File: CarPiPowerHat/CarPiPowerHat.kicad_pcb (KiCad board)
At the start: 4 copper layers, 96 x 85 mm, 124 parts, among them IC1 AP2331TDSA-7, J1 HDMI_A_1.4, J10 Conn_01x02_Male, J2 1-84953-5, J3 40HAT, J4 Conn_02x03_Counter_Clockwise, J5 USB_A, J6 1-84953-5, J7 HDMI_A_1.4, J8 AudioJack2_Ground, J9 Conn_01x04, Q1 DMMT5401, Q2 DMG2305UX, Q3 DMP3013SFV-7, Q4 DMG2305, U1 AP64501SP-13, U2 CAT24C32, U3 LM3480-5.0, U4 ATtiny45V-10X, U5 PCF85063AT/AAZ, U7 AP2112-3.3K, U8 UDA1334ATS, Y1 X32K768S301

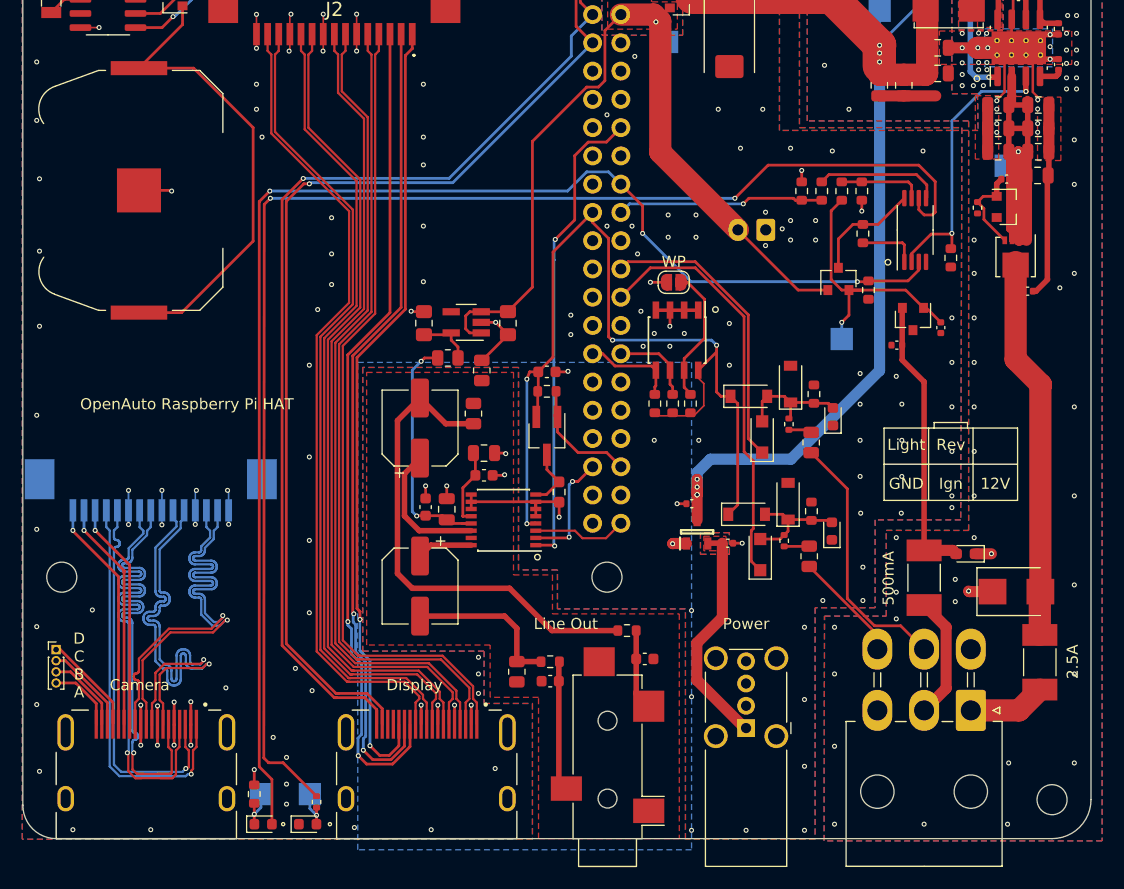
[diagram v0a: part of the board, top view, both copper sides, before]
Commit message: updated layout
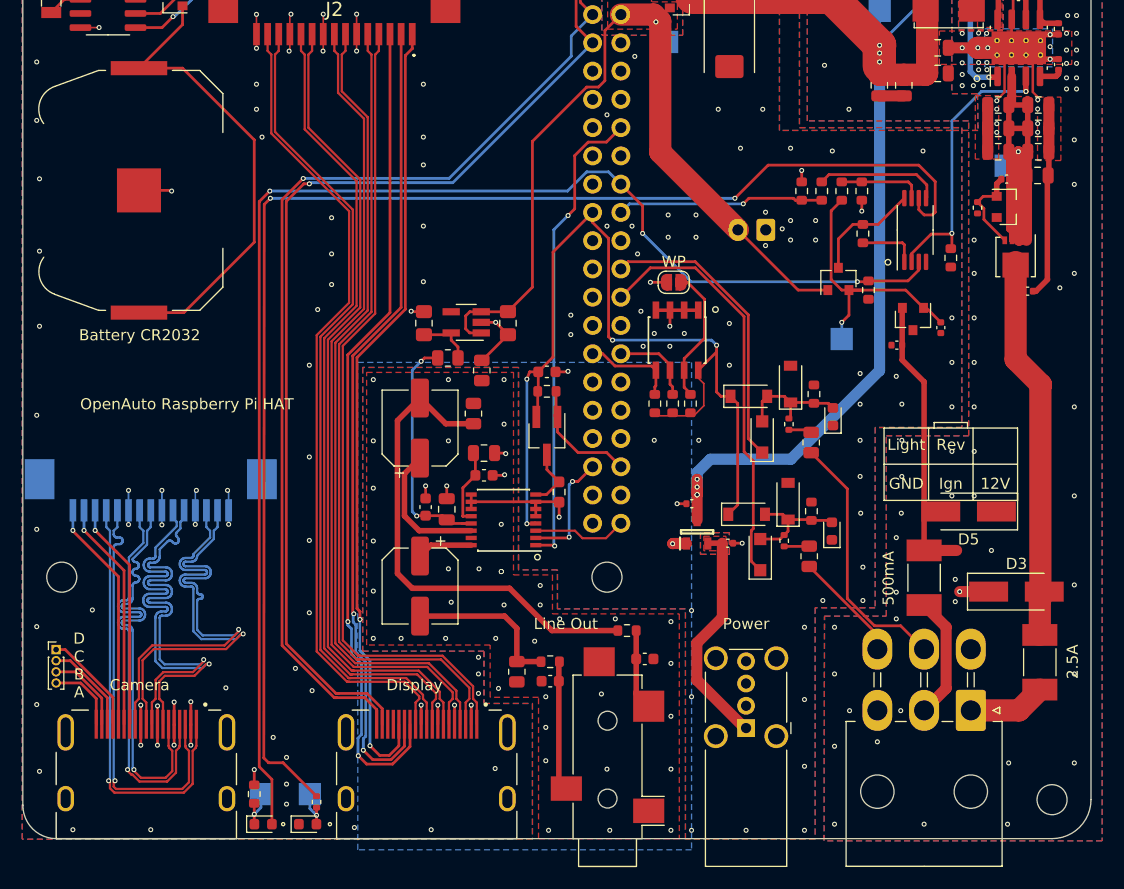
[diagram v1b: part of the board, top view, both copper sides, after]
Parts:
- D3: footprint Diode_SMD:D_SMB -> Diode_SMD:D_SMA_Handsoldering
- D5: footprint Diode_SMD:D_0603_1608Metric_Pad1.05x0.95mm_HandSolder -> Diode_SMD:D_SMA_Handsoldering
- moved D5 3.81 mm to (163.0, 87.1)
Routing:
- net /HDMI Connector Camera/D1-: track 46.5 -> 38.6 mm
- net /HDMI Connector Camera/D1+: track 45.8 -> 38.6 mm
- net /HDMI Connector Camera/D2-: track 34.6 -> 38.6 mm
- net /HDMI Connector Camera/D0-: track 35.8 -> 39.8 mm
- net GND: track 158.1 -> 154.6 mm, vias 237 -> 238
- net /HDMI Connector Camera/D0+: track 36.7 -> 39.8 mm
- net /HDMI Connector Camera/CK-: track 36.6 -> 38.7 mm
- net /HDMI Connector Camera/D2+: track 36.6 -> 38.6 mm
- net /HDMI Connector Camera/CK+: track 37.3 -> 38.6 mm
- net AGND: vias 4 -> 42
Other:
- board text added: "Battery CR2032"

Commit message: added some more documentation
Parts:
- moved D5 0.18 mm to (162.8, 87.0), turned to -90 degrees
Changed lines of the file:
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@@
-(kicad_pcb (version 20210424) (generator pcbnew)
+(kicad_pcb (version 20210606) (generator pcbnew)
   (general
     (thickness 1.6)
@@
   )
   (footprint "Diode_SMD:D_SMA_Handsoldering" (layer "F.Cu")
-    (at 163.000035 87.09999 180)
+    (at 162.836035 87.03599 -90)
     (descr "Diode SMA (DO-214AC) Handsoldering")
     (tags "Diode SMA (DO-214AC) Handsoldering")
@@
     (property "Sheetname" "Power Control")
     (attr smd)
-    (fp_text reference "D5" (at 0 -2.5 180) (layer "F.SilkS")
+    (fp_text reference "D5" (at 0 -2.5 90) (layer "F.SilkS")
       (effects (font (size 1 1) (thickness 0.15)))
     )
-    (fp_text value "D_TVS" (at 0 2.6 180) (layer "F.Fab")
+    (fp_text value "D_TVS" (at 0 2.6 90) (layer "F.Fab")
       (effects (font (size 1 1) (thickness 0.15)))
     )
-    (fp_text user "${REFERENCE}" (at 0 -2.5 180) (layer "F.Fab")
+    (fp_text user "${REFERENCE}" (at 0 -2.5 90) (layer "F.Fab")
       (effects (font (size 1 1) (thickness 0.15)))
     )
@@
     (fp_line (start -2.3 1.5) (end -2.3 -1.5) (layer "F.Fab") (width 0.1))
     (fp_line (start 0.50118 0.00102) (end 1.4994 0.00102) (layer "F.Fab") (width 0.1))
-    (pad "1" smd rect locked (at -2.5 0 180) (size 3.5 1.8) (layers "F.Cu" "F.Paste" "F.Mask")
+    (pad "1" smd rect locked (at -2.5 0 270) (size 3.5 1.8) (layers "F.Cu" "F.Paste" "F.Mask")
       (net 1 "GND") (pinfunction "A1") (pintype "passive"))
-    (pad "2" smd rect locked (at 2.5 0 180) (size 3.5 1.8) (layers "F.Cu" "F.Paste" "F.Mask")
+    (pad "2" smd rect locked (at 2.5 0 270) (size 3.5 1.8) (layers "F.Cu" "F.Paste" "F.Mask")
       (net 7 "Net-(C20-Pad1)") (pinfunction "A2") (pintype "passive"))
     (model "${KICAD6_3DMODEL_DIR}/Diode_SMD.3dshapes/D_SMA.wrl"
@@
   (via (at 87.5 88.27) (size 0.45) (drill 0.25) (layers "F.Cu" "B.Cu") (net 1))
   (via (at 138.10007 103.74999) (size 0.45) (drill 0.25) (layers "F.Cu" "B.Cu") (free) (net 1))
-  (via (at 163.5 81.7) (size 0.45) (drill 0.25) (layers "F.Cu" "B.Cu") (free) (net 1))
+  (via (at 163.852035 81.7) (size 0.45) (drill 0.25) (layers "F.Cu" "B.Cu") (free) (net 1))
   (via (at 134.4 66.5) (size 0.45) (drill 0.25) (layers "F.Cu" "B.Cu") (free) (net 1))
   (via (at 136.15 72.25) (size 0.45) (drill 0.25) (layers "F.Cu" "B.Cu") (free) (net 1))
@@
   (via (at 149.900628 95.100658) (size 0.45) (drill 0.25) (layers "F.Cu" "B.Cu") (free) (net 1))
   (via (at 157.5 32.7) (size 0.45) (drill 0.25) (layers "F.Cu" "B.Cu") (free) (net 1))
-  (via (at 163.5 85.7) (size 0.45) (drill 0.25) (layers "F.Cu" "B.Cu") (free) (net 1))
+  (via (at 165.376035 84.49599) (size 0.45) (drill 0.25) (layers "F.Cu" "B.Cu") (free) (net 1))
   (via (at 79.25 51.95) (size 0.45) (drill 0.25) (layers "F.Cu" "B.Cu") (free) (net 1))
   (via (at 162.200035 94.29999) (size 0.45) (drill 0.25) (layers "F.Cu" "B.Cu") (free) (net 1))
@@
   (via (at 169.205 53.017) (size 0.45) (drill 0.25) (layers "F.Cu" "B.Cu") (free) (net 1))
   (via (at 100.5 107.4) (size 0.45) (drill 0.25) (layers "F.Cu" "B.Cu") (free) (net 1))
-  (via (at 161.5 85.7) (size 0.45) (drill 0.25) (layers "F.Cu" "B.Cu") (free) (net 1))
+  (via (at 160.296035 84.49599) (size 0.45) (drill 0.25) (layers "F.Cu" "B.Cu") (free) (net 1))
   (via (at 157 77.45) (size 0.45) (drill 0.25) (layers "F.Cu" "B.Cu") (free) (net 1))
   (via (at 148.250035 103.99999) (size 0.45) (drill 0.25) (layers "F.Cu" "B.Cu") (free) (net 1))

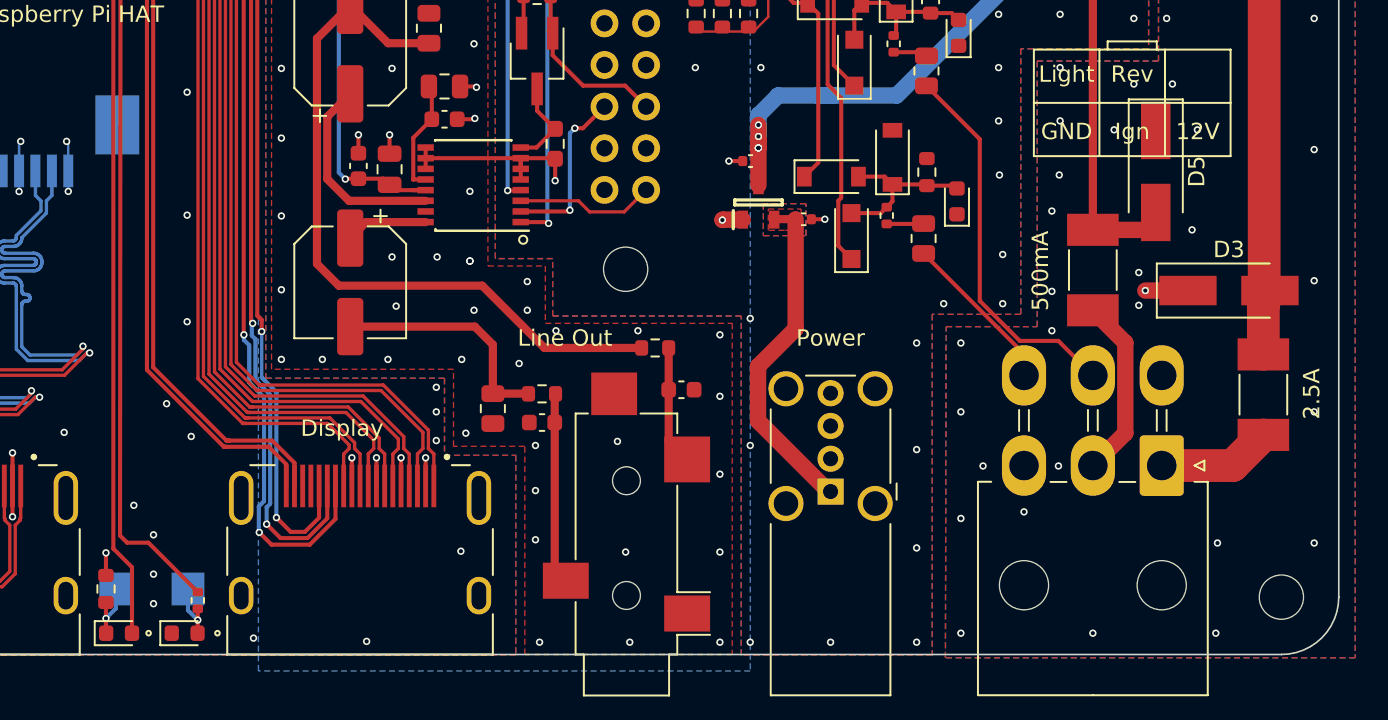
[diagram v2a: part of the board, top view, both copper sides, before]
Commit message: Removed TVS diodes for now, fixed DRC issues
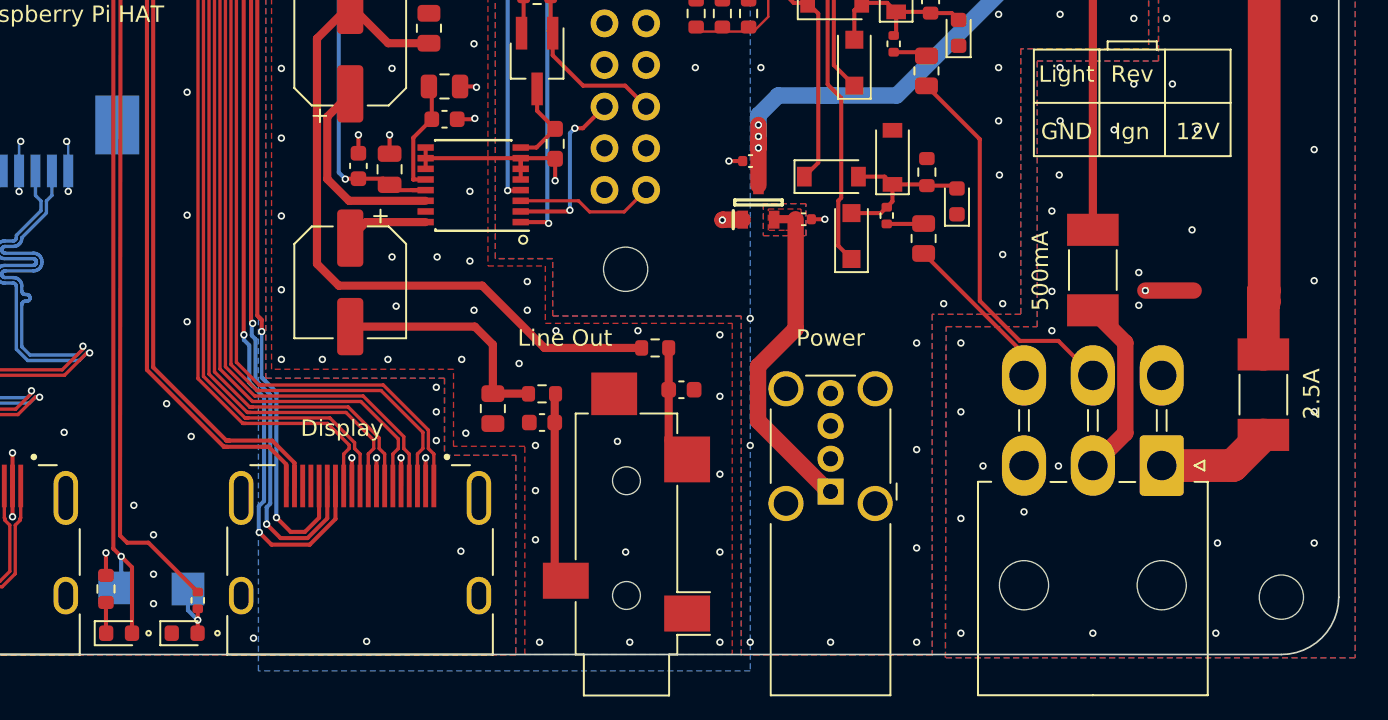
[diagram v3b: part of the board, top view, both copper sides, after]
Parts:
- removed D3, D5: D_TVS, Diode_SMD:D_SMA_Handsoldering
- moved TP7 0.09 mm to (99.3, 112.4)
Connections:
- net /RTC Clock/SDA renamed /HDMI Connector Display/A
- net /i2s_dac/+5v renamed /PSU/+5v
- TP7 pad 1: Net-(D1-Pad1) -> PWR_SENSE_OUT
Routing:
- net Net-(C20-Pad1): track 25.5 -> 22.6 mm
- net Net-(D1-Pad1): track 3.93 -> 1.88 mm, vias 1 -> 0
- net PWR_SENSE_OUT: track 123.6 -> 125.5 mm, vias 3 -> 4
- net /Power Control/VO: track 25.1 -> 26.3 mm
- net AGND: vias 42 -> 41
- net /PSU/P5V: vias 8 -> 7

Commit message: Finished Layout
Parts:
- removed D12, D13: D_Schottky, Diode_SMD:D_SOD-123
- removed D14: D, Diode_SMD:D_SOD-123F
- removed FB2, FB3: FerriteBead, Resistor_SMD:R_0805_2012Metric
- added D3: SMBJ33A, Diode_SMD:D_SMB, F.Cu at (167.3, 93.0)
- added D5: BAT54S, Package_TO_SOT_SMD:SOT-23, F.Cu at (143.0, 79.5)
- C1, C11, C2, C3, C5, C6, C7: value 10u 35v -> 10uF 35v
- C15, C16, C17, C18: value 10u -> 10uF
- C22, C23: value 10u -> 10uF; footprint Resistor_SMD:R_0603_1608Metric -> Capacitor_SMD:C_0603_1608Metric
- C28, C31: footprint Capacitor_SMD:C_0805_2012Metric_Pad1.18x1.45mm_HandSolder -> Capacitor_SMD:C_0805_2012Metric
- D1: value LED -> LED Red
- D10: value D -> D_Schottky 15mA; footprint Diode_SMD:D_SOD-123F -> Diode_SMD:D_SOD-323
- D11, D7: value D_TVS -> TPGBLC12C; footprint Diode_SMD:D_0603_1608Metric -> Diode_SMD:D_SOD-323
- D2: value LED -> LED Green
- D6: value D_Dual_CommonCathode_AAK_Parallel -> BAT54C-7-F
- D8: value D_Schottky -> D_Schottky 15mA; footprint Diode_SMD:D_SOD-123 -> Diode_SMD:D_SOD-323
- D9: value D_Schottky -> BAT54S; footprint Diode_SMD:D_SOD-123 -> Package_TO_SOT_SMD:SOT-23
- R11: footprint Resistor_SMD:R_0603_1608Metric -> Resistor_SMD:R_0402_1005Metric
- moved D9 10.9 mm to (143.0, 85.7), turned to 180 degrees
- moved R21 6.56 mm to (148.5, 83.5), turned to 0 degrees
- moved D11 5.44 mm to (146.3, 85.7)
- moved R13 5.32 mm to (159.3, 66.7), turned to 0 degrees
- moved D7 4.65 mm to (146.3, 79.5)
- moved C22 3.07 mm to (148.3, 79.5), turned to -90 degrees
- moved D10 2.90 mm to (142.8, 82.7), turned to 0 degrees
- moved R20 2.59 mm to (148.5, 77.2), turned to 0 degrees
- moved C23 1.47 mm to (148.3, 85.7), turned to -90 degrees
- moved C20 1.07 mm to (157.5, 72.6), turned to 0 degrees
- moved R11 0.60 mm to (98.8, 113.1)
- moved D8 0.56 mm to (142.8, 76.5)
- moved R5 0.36 mm to (164.0, 60.1)
- moved D6 0.30 mm to (151.3, 66.5)
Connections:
- net /RTC Clock/SCL renamed /HDMI Connector Display/B
- D10 pad 1: /Raspberry Pi/BCM25 -> /Light Input/OUT
- D10 pad 2: Net-(C22-Pad1) -> Net-(D10-Pad2)
- D6 pad 1: /PSU/+5v -> /Power Control/VO
- D6 pad 2: /Power Control/VO -> /PSU/+5v
- D8 pad 1: /+3.3v -> /Raspberry Pi/BCM25
- D8 pad 2: Net-(C22-Pad1) -> Net-(D5-Pad3)
- D9 pad 1: Net-(C22-Pad1) -> GND
- D9 pad 2: GND -> /+3.3v
- R20 pad 2: Net-(FB2-Pad2) -> CAR_REVERSE
- R21 pad 2: Net-(FB3-Pad2) -> CAR_LIGHT
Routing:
- net /Light Input/OUT: track 37.5 -> 27.4 mm
- net CAR_LIGHT: track 9.97 -> 19.7 mm
- net Net-(C22-Pad1): track 10.3 -> 3.70 mm
- net Net-(C23-Pad1): track 10.1 -> 3.70 mm
- net /Raspberry Pi/BCM25: track 26.6 -> 20.5 mm
- net CAR_REVERSE: track 23.7 -> 28.1 mm
- net /PSU/+5v: track 81.1 -> 85.3 mm
- net Net-(D5-Pad3): track 0.00 -> 3.72 mm
- net Net-(D10-Pad2): track 0.00 -> 3.72 mm
- net GND: track 154.6 -> 157.9 mm, vias 238 -> 268
- net Net-(FB3-Pad2): track 2.26 -> 0.00 mm
- net Net-(FB2-Pad2): track 2.09 -> 0.00 mm
- net /+3.3v: track 123.6 -> 122.5 mm
- net PWR_SENSE_OUT: track 125.5 -> 126.5 mm
- added copper zone on B.Cu, net AGND
- added copper zone on In2.Cu, net AGND
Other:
- board text added: "Board thickness : 1.56mm Finished copper weight inners : 1oz Finished copper weight outers : 1oz Board finish : OSP Material type : FR4 Colour of solder resists : Green Colour of silk screens : White Only on the top side Board to : UL94-V0 TG >=130 50R trace width 0.13mm@ 3GHz 90R diff pair width 0.147 spacing 0.253mm @ 2.5GHz 100R diff pair width 0.127 spacing 0.253mm @ 2GHz"
